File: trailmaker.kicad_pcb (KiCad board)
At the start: 2 copper layers, 13 parts, among them SW1 SW_Push, SW2 SW_Push, SW3 SW_Push, SW4 SW_Push, U1 XIAO-RP2040-DIP

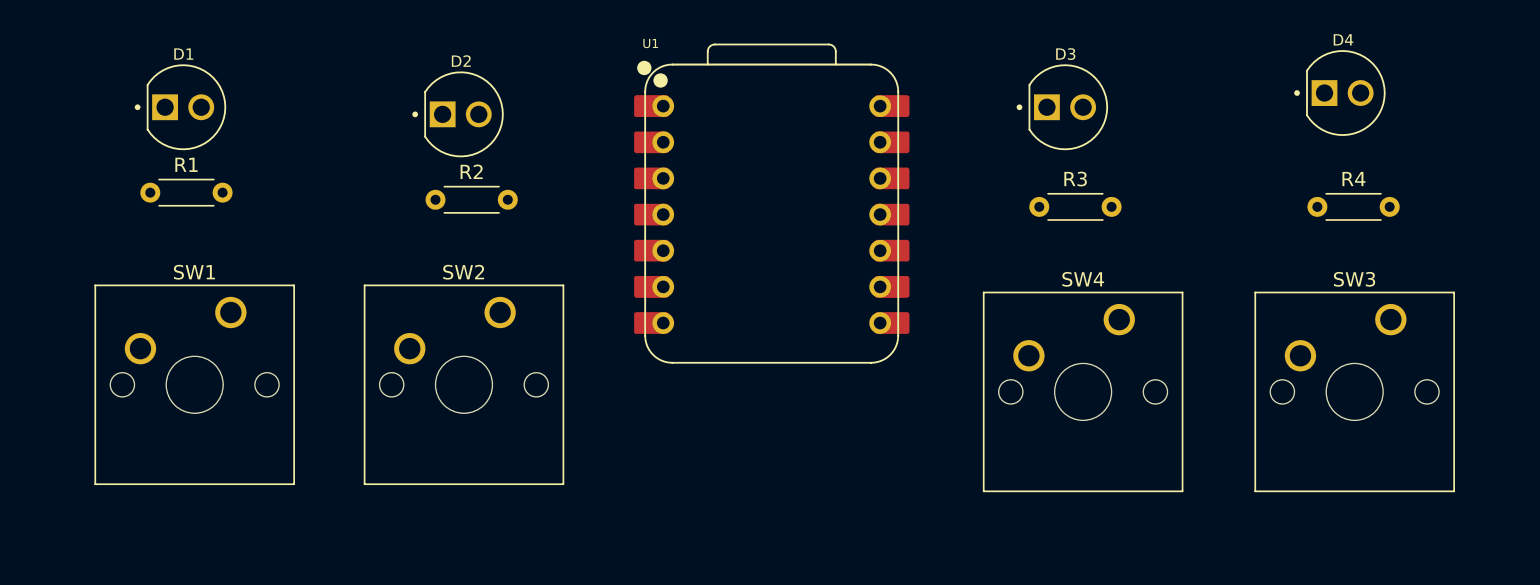
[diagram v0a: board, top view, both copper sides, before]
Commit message: created PCB layout and Arduino code
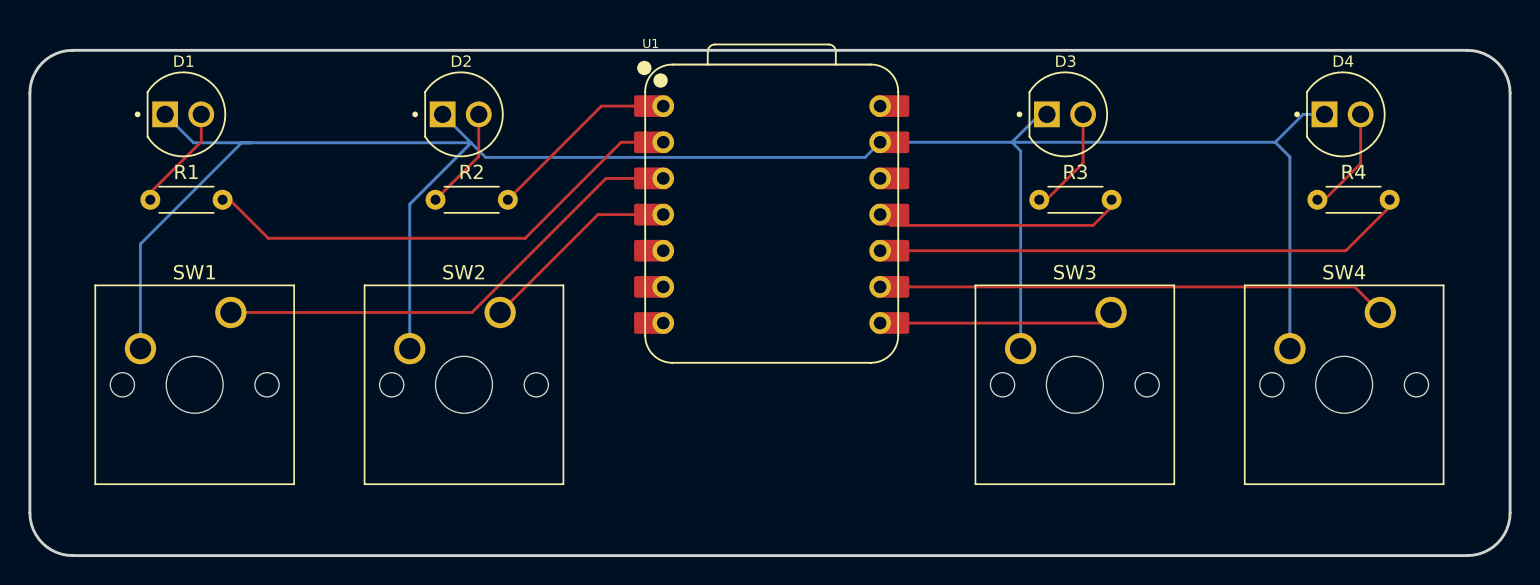
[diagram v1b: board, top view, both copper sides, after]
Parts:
- SW1, SW2, SW3, SW4: footprint Button_Switch_Keyboard:SW_Cherry_MX_1.00u_PCB -> footprints:SW_Cherry_MX_1.00u_PCB_Rubey
- moved SW3 19.7 mm to (157.5, 95.9)
- moved SW4 18.3 mm to (176.4, 95.9)
- moved D4 1.50 mm to (173.7, 82.0)
- moved D1 0.50 mm to (92.3, 82.0)
- moved D3 0.50 mm to (154.2, 82.0)
- moved R1 0.50 mm to (90.0, 88.0)
- moved R3 0.50 mm to (152.4, 88.0)
- moved R4 0.50 mm to (172.0, 88.0)
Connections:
- U1 pad 1: LED1 -> LED2
- U1 pad 10: LED3 -> LED4
- U1 pad 11: LED4 -> LED3
- U1 pad 2: LED2 -> LED1
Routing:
- net GND: track 0.00 -> 154.2 mm
- net LED4: track 0.00 -> 37.1 mm
- net LED1: track 0.00 -> 35.1 mm
- net button4: track 0.00 -> 35.1 mm
- net button1: track 0.00 -> 34.3 mm
- net LED3: track 0.00 -> 17.1 mm
- net button3: track 0.00 -> 15.7 mm
- net button2: track 0.00 -> 14.3 mm
- net LED2: track 0.00 -> 13.6 mm
- net Net-(D3-PadA): track 0.00 -> 8.28 mm
- net Net-(D4-PadA): track 0.00 -> 7.76 mm
- net Net-(D1-PadA): track 0.00 -> 7.48 mm
- net Net-(D2-PadA): track 0.00 -> 7.26 mm
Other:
- board outline added: 104 x 35.5 mm

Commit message: Code bug fixing and PCB finalization
Added silkscreen to PCB and exported gerber and dril file for JLC PCB
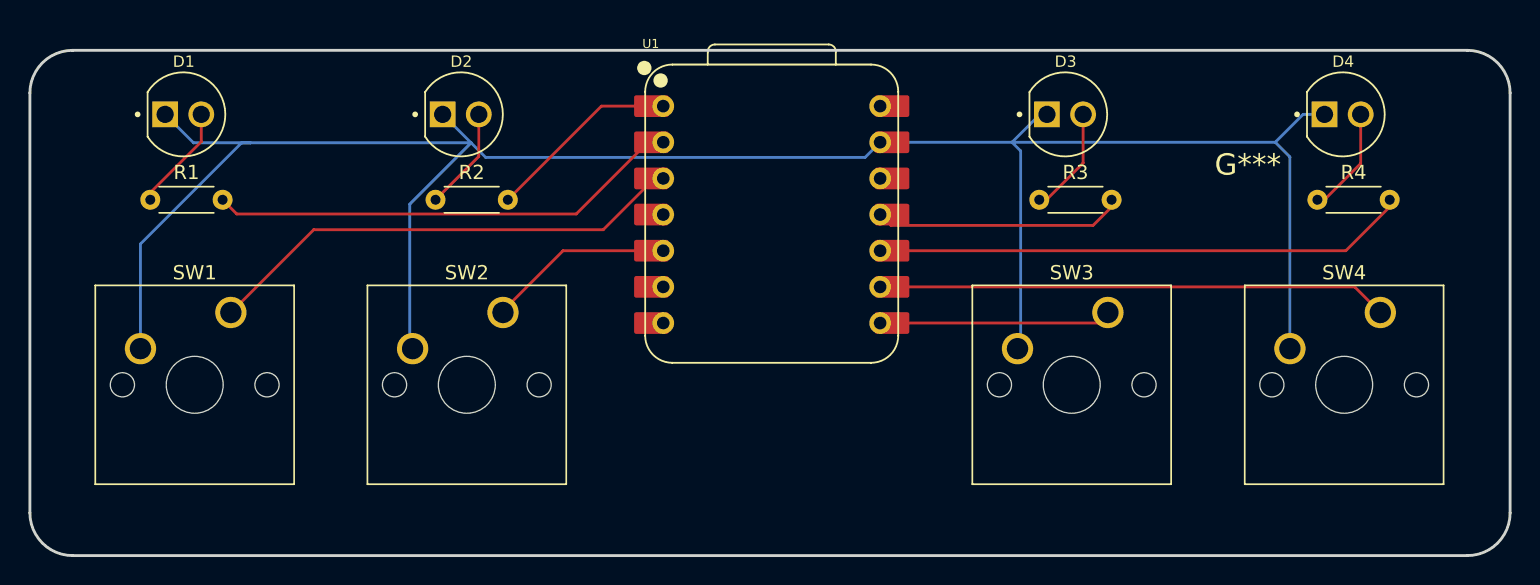
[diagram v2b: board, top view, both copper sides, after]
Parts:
- added G***: LOGO, KiCAD_models:ReactorSign, B.Cu at (133.6, 99.5)
- added G***: LOGO, KiCAD_models:OrpheusFlag, B.Cu at (167.1, 85.5)
- moved SW3 0.22 mm to (157.2, 95.9)
- moved SW2 0.20 mm to (114.7, 95.9)
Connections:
- U1 pad 4: button2 -> unconnected-(U1-GPIO29/ADC3/A3-Pad4)
- U1 pad 5: unconnected-(U1-GPIO6/SDA-Pad5) -> button2
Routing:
- net LED1: track 35.1 -> 33.5 mm
- net button2: track 14.3 -> 13.2 mm
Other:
- board text added: "Made by Rubey"
- board text added: "REACTOR V1.0"
